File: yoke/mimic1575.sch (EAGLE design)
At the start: 33 parts, among them P1 1K, P2 20, P3 1K, P4 20, U1 CD74HCT75, U10 DG417B, U11 OPA2340N, U12 CD74HCT123, U2 CD74HC573E, U3 CD74HC573E, U4 CD74HC573E, U5 AD7533, U6 AD7533, U7 DG417B, U8 OPA2340N

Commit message: more changes
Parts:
- removed C1, C5: 10pF, keiths:C-0.1
- removed C10, C9: 27pF, keiths:C-0.1
- removed C3, C6: 1000pF, keiths:C-0.1
- removed C7: 3.3uF, keiths:MKS2B043301H00
- removed P1, P3: 1K, keiths:POT-3006P
- removed P2, P4: 20, keiths:POT-3006P
- removed R1, R10: 332, keiths:R-1/4WATT
- removed R16: 1M, keiths:R-1/4WATT
- removed R17, R9: 1.0K, keiths:R-1/4WATT
- removed R4: 2.0K, keiths:R-1/4WATT
- removed U1: CD74HCT75, keiths:CD74HCT75
- removed U10, U7: DG417B, keiths:DG417B
- removed U11, U8: OPA2340N, keiths:OPA2340N
- removed U12: CD74HCT123, keiths:CD74HCT123
- removed U2, U3, U4: CD74HC573E, keiths:CD74HC573E
- removed U5, U6: AD7533, keiths:AD7533
- added C2: 0.022 uF, keiths:ECQ-E2223JF
- added P6: 44PINEDGE, keiths:44PINEDGE
- added Q1, Q14, Q15, Q20, Q6: 2N3904, keiths:2N3904
- added Q10, Q16, Q17, Q18, Q19, Q7: 2N2907, keiths:2N2907
- added Q11, Q13: 2N3906, keiths:2N3906
- added R12: 470, keiths:AXIALRESISTORQUARTER_WATT
- added R13: 560, keiths:AXIALRESISTORQUARTER_WATT
- added R14, R19: 27, keiths:AXIALRESISTORQUARTER_WATT
- added R21: 120, keiths:AXIALRESISTORQUARTER_WATT
- C4: value 3.3uF -> 0.022 uF; device keiths:MKS2B043301H00 -> keiths:ECQ-E2223JF; PN MKS2B043301H00MSSD -> ECQ-E2223JFB
- R11: value 220 -> 1500; device keiths:R-1/4WATT -> keiths:AXIALRESISTORQUARTER_WATT
- R3: value 220 -> 27; device keiths:R-1/4WATT -> keiths:AXIALRESISTORQUARTER_WATT
- R5: value 2.0K -> 27; device keiths:R-1/4WATT -> keiths:AXIALRESISTORQUARTER_WATT
- R8: value 1M -> 120; device keiths:R-1/4WATT -> keiths:AXIALRESISTORQUARTER_WATT
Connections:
- removed net +15V: U10.V+, U11P.V+, U5.VDD, U6.VDD, U7.V+, U8P.V+
- removed net D0: U1.1D1, U1.2D1
- removed net D1: U1.1D0, U1.2D0
- removed net D2: U2.D7, U3.D7, U4.D7
- removed net D3: U2.D6, U3.D6, U4.D6
- removed net D4: U2.D5, U3.D5, U4.D5
- removed net D5: U2.D4, U3.D4, U4.D4
- removed net D6: U2.D3, U3.D3, U4.D3
- removed net D7: U2.D2, U3.D2, U4.D2
- removed net D8: U2.D1, U3.D1, U4.D1
- removed net D9: U2.D0, U3.D0, U4.D0
- removed net LEX: U1.!1LE, U3.LE
- removed net LEX1: U12.1B
- removed net LEY: U1.!2LE, U2.LE
- removed net LEY1: U12.2B
- removed net LE_CTR: U4.LE
- removed net N$1: R9.P$2, U11B.-IN, U11B.OUT
- removed net N$10: U2.Q3, U6.D6
- removed net N$11: U2.Q4, U6.D5
- removed net N$12: U2.Q5, U6.D4
- removed net N$13: U2.Q6, U6.D3
- removed net N$14: U2.Q7, U6.D2
- removed net N$15: U4.Q7
- removed net N$16: U4.Q6
- removed net N$17: U4.Q5
- removed net N$18: U4.Q4
- removed net N$19: U4.Q3
- removed net N$2: C9.2, R4.P$1, U12.1R/C
- removed net N$20: U4.Q2
- removed net N$21: U4.Q1
- removed net N$23: C1.2, R1.P$1, U10.S, U11A.OUT
- removed net N$25: U3.Q0, U5.D9
- removed net N$29: U3.Q4, U5.D5
- removed net N$3: U1.1Q0, U5.D1
- removed net N$4: U1.1Q1, U5.D0
- removed net N$40: C4.1, P2.A, R9.P$1
- removed net N$42: C3.1, R3.P$1, R8.P$1, U11B.+IN
- removed net N$44: C5.2, R10.P$1, U7.S, U8A.OUT
- removed net N$45: C5.1, U6.IO1, U8A.-IN
- removed net N$46: U6.IO2, U8A.+IN
- removed net N$47: R10.P$2, U6.RFB
- removed net N$48: C10.1, U12.2C
- removed net N$49: C6.1, R11.P$1, R16.P$1, U8B.+IN
- removed net N$5: C1.1, U11A.-IN, U5.IO1
- removed net N$50: R17.P$2, U8B.-IN, U8B.OUT
- removed net N$51: R11.P$2, U7.D
- removed net N$53: P3.A, U6.VREF
- removed net N$56: C7.1, P4.A, R17.P$1
- removed net N$6: U11A.+IN, U5.IO2
- removed net N$7: U2.Q0, U6.D9
- removed net N$8: U2.Q1, U6.D8
- removed net N$9: U2.Q2, U6.D7
- removed net VREF: P1.E, P1.S, P3.E, P3.S
- removed net XOUT: C4.2, P2.E, P2.S
- removed net X_GATE: U10.IN, U12.1Q
- removed net YOUT: C7.2, P4.E, P4.S
- removed net Y_GATE: U12.2Q, U7.IN
- new net +10V: P6.A, R12.P$2, R19.P$2, R5.P$2, R8.P$2
- new net +50V: P6.E
- new net GATE: Q20.B
- new net INPUT: Q7.B
- new net W_IN: P6.W
- new net Z_IN: P6.Z
- net +5V: now also P6.F; no longer R4.P$2, R5.P$2, U1.+5V, U10.VL, U12.!1CLR, U12.!2CLR, U12.+5V, U2.+5V, U3.+5V, U4.+5V, U7.VL
- net -15V: now also C2.1, C4.1, P6.C, R13.P$1, R14.P$1, R21.P$1, R3.P$1; no longer U10.V-, U11P.V-, U7.V-, U8P.V-
- net GND: now also P6.D; no longer C3.2, C6.2, R16.P$2, R8.P$2, U1.GND, U10.GND, U12.!1A, U12.!2A, U12.GND, U2.!OE, U2.GND, U3.!OE, U3.GND, U4.!OE, U4.GND, U5.GND, U6.GND, U7.GND
- net N$22: now also Q14.B, Q6.B; no longer U4.Q0
- net N$24: now also Q17.E, R5.P$1; no longer P1.A, U5.VREF
- net N$26: now also Q18.E, R8.P$1; no longer U3.Q1, U5.D8
- net N$27: now also Q14.E, R3.P$2; no longer U3.Q2, U5.D7
- net N$28: now also Q6.E, R14.P$2; no longer U3.Q3, U5.D6
- net N$30: now also Q18.C, Q19.B, Q7.E; no longer U3.Q5, U5.D4
- net N$31: now also C2.2, Q7.C, R13.P$2; no longer U3.Q6, U5.D3
- net N$32: now also Q10.B, Q14.C, Q17.B, Q17.C, Q18.B; no longer U3.Q7, U5.D2
- net N$33: now also Q10.E, R19.P$1; no longer C9.1, U12.1C
- net N$34: now also Q6.C, R11.P$1; no longer R3.P$2, U10.D
- net N$35: now also Q10.C, Q19.E; no longer U1.2Q0, U6.D1
- net N$36: now also C4.2, Q19.C, R21.P$2; no longer U1.2Q1, U6.D0
- net N$37: now also Q20.E, R11.P$2; no longer C10.2, R5.P$1, U12.2R/C
- net N$38: now also Q20.C, R12.P$1; no longer R1.P$2, U5.RFB
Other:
- note added: "Follow and Hold"

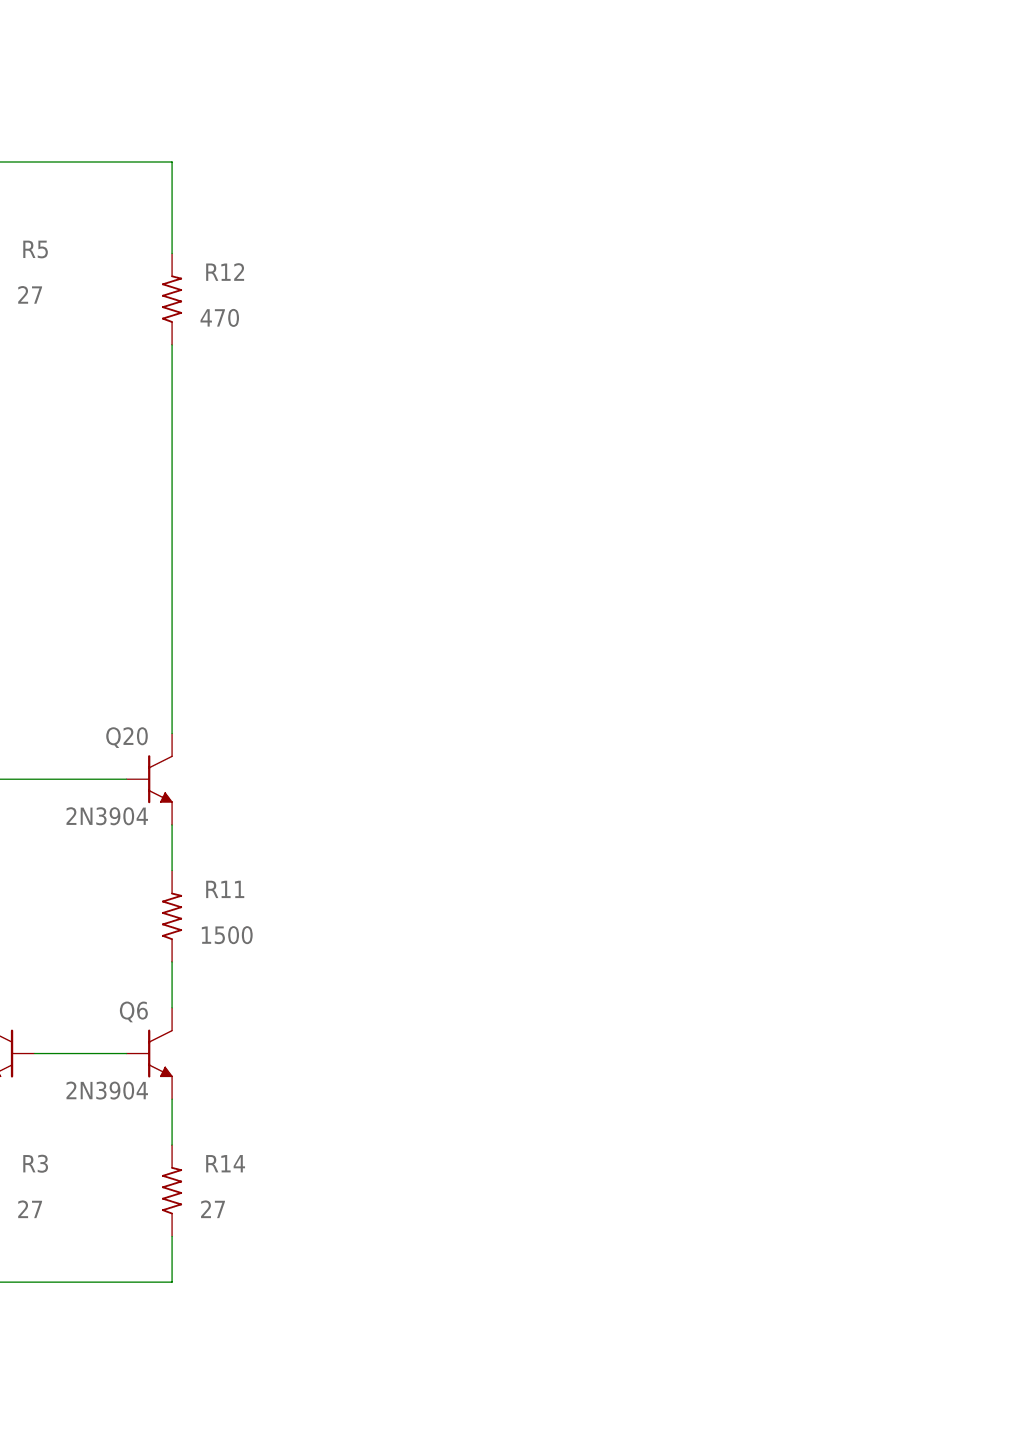
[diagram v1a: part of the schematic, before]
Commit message: LTspice files added
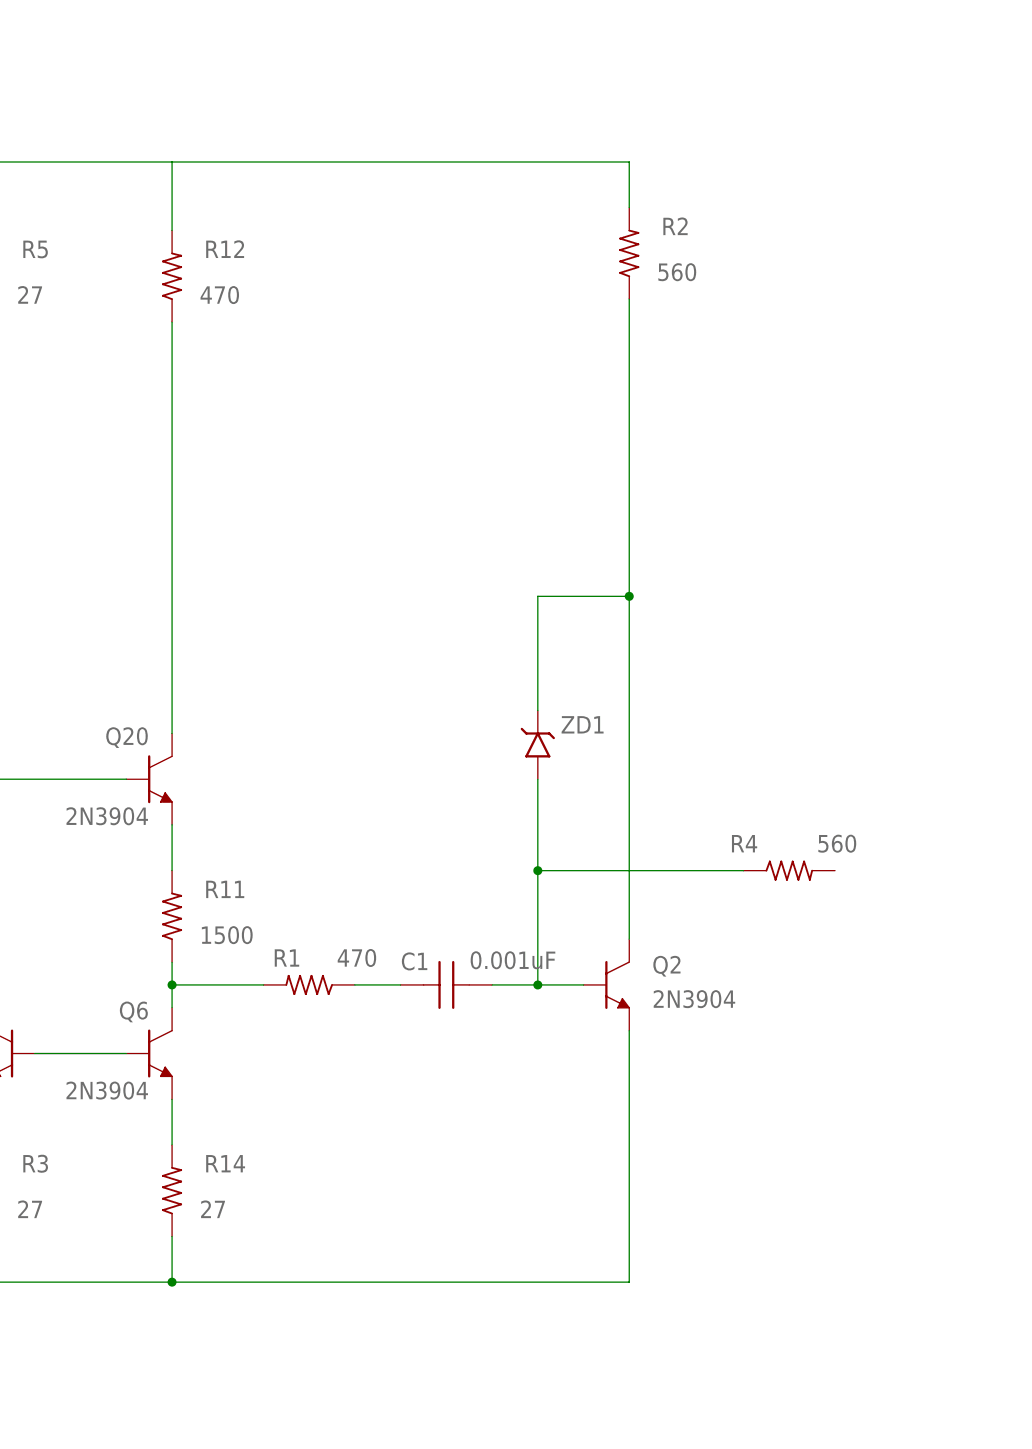
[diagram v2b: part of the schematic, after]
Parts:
- added C1: 0.001uF, keiths:CAP0.1UF100V
- added Q2: 2N3904, keiths:2N3904
- added R1: 470, keiths:AXIALRESISTORQUARTER_WATT
- added R2, R4: 560, keiths:AXIALRESISTORQUARTER_WATT
- added ZD1: (no value), keiths:1N754A
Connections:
- new net N$1: C1.1, R1.P$1
- new net N$2: Q2.C, R2.P$1, ZD1.C
- new net N$3: C1.2, Q2.B, R4.P$1, ZD1.A
- net +10V: now also R2.P$2
- net -15V: now also Q2.E
- net N$34: now also R1.P$2
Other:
- moved on the sheet: R12
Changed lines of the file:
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@@
 <attribute name="PN" value="2N3904"/>
 </part>
+<part name="C1" library="keiths" deviceset="CAP0.1UF100V" device="" value="0.001uF"/>
+<part name="R1" library="keiths" deviceset="AXIALRESISTOR" device="QUARTER_WATT" value="470"/>
+<part name="Q2" library="keiths" deviceset="2N3904" device="">
+<attribute name="PN" value="2N3904"/>
+</part>
+<part name="R2" library="keiths" deviceset="AXIALRESISTOR" device="QUARTER_WATT" value="560"/>
+<part name="ZD1" library="keiths" deviceset="1N754A" device=""/>
+<part name="R4" library="keiths" deviceset="AXIALRESISTOR" device="QUARTER_WATT" value="560"/>
 </parts>
 <sheets>
@@
 <attribute name="VALUE" x="229.108" y="182.372" size="1.9304" layer="96" font="vector" ratio="10"/>
 </instance>
-<instance part="R12" gate="G$1" x="226.06" y="254" smashed="yes" rot="R180">
-<attribute name="NAME" x="229.616" y="256.032" size="1.9304" layer="95" font="vector" ratio="10"/>
-<attribute name="VALUE" x="229.108" y="250.952" size="1.9304" layer="96" font="vector" ratio="10"/>
+<instance part="R12" gate="G$1" x="226.06" y="256.54" smashed="yes" rot="R180">
+<attribute name="NAME" x="229.616" y="258.572" size="1.9304" layer="95" font="vector" ratio="10"/>
+<attribute name="VALUE" x="229.108" y="253.492" size="1.9304" layer="96" font="vector" ratio="10"/>
 </instance>
 <instance part="R14" gate="G$1" x="226.06" y="154.94" smashed="yes" rot="R180">
@@
 <attribute name="VALUE" x="162.56" y="289.56" size="1.9304" layer="96" font="vector" ratio="10"/>
 <attribute name="PN" x="154.94" y="294.64" size="1.778" layer="96" display="off"/>
+</instance>
+<instance part="C1" gate="G$1" x="256.54" y="177.8" smashed="yes" rot="R90">
+<attribute name="NAME" x="251.46" y="179.451" size="1.9304" layer="95" font="vector" ratio="10"/>
+<attribute name="VALUE" x="259.08" y="179.578" size="1.9304" layer="96" font="vector" ratio="10"/>
+</instance>
+<instance part="R1" gate="G$1" x="241.3" y="177.8" smashed="yes" rot="R270">
+<attribute name="NAME" x="237.236" y="179.832" size="1.9304" layer="95" font="vector" ratio="10"/>
+<attribute name="VALUE" x="244.348" y="179.832" size="1.9304" layer="96" font="vector" ratio="10"/>
+</instance>
+<instance part="Q2" gate="G1" x="274.32" y="177.8" smashed="yes">
+<attribute name="NAME" x="279.4" y="179.07" size="1.9304" layer="95" font="vector" ratio="10"/>
+<attribute name="VALUE" x="279.4" y="175.26" size="1.9304" layer="96" font="vector" ratio="10"/>
+<attribute name="PN" x="274.32" y="177.8" size="1.778" layer="96" display="off"/>
+</instance>
+<instance part="R2" gate="G$1" x="276.86" y="259.08" smashed="yes" rot="R180">
+<attribute name="NAME" x="280.416" y="261.112" size="1.9304" layer="95" font="vector" ratio="10"/>
+<attribute name="VALUE" x="279.908" y="256.032" size="1.9304" layer="96" font="vector" ratio="10"/>
+</instance>
+<instance part="ZD1" gate="G$1" x="266.7" y="203.2"/>
+<instance part="R4" gate="G$1" x="294.64" y="190.5" smashed="yes" rot="R90">
+<attribute name="NAME" x="288.036" y="192.532" size="1.9304" layer="95" font="vector" ratio="10"/>
+<attribute name="VALUE" x="297.688" y="192.532" size="1.9304" layer="96" font="vector" ratio="10"/>
 </instance>
 </instances>
@@
 <wire x1="205.74" y1="149.86" x2="205.74" y2="144.78" width="0.1524" layer="91"/>
 <junction x="205.74" y="144.78"/>
+<pinref part="Q2" gate="G1" pin="E"/>
+<wire x1="226.06" y1="144.78" x2="276.86" y2="144.78" width="0.1524" layer="91"/>
+<wire x1="276.86" y1="144.78" x2="276.86" y2="172.72" width="0.1524" layer="91"/>
+<junction x="226.06" y="144.78"/>
 </segment>
 </net>
@@
 <wire x1="170.18" y1="269.24" x2="205.74" y2="269.24" width="0.1524" layer="91"/>
 <wire x1="205.74" y1="269.24" x2="226.06" y2="269.24" width="0.1524" layer="91"/>
-<wire x1="226.06" y1="269.24" x2="226.06" y2="259.08" width="0.1524" layer="91"/>
 <junction x="170.18" y="269.24"/>
 <pinref part="R5" gate="G$1" pin="P$2"/>
+<wire x1="226.06" y1="269.24" x2="226.06" y2="261.62" width="0.1524" layer="91"/>
 <wire x1="205.74" y1="261.62" x2="205.74" y2="269.24" width="0.1524" layer="91"/>
 <junction x="205.74" y="269.24"/>
+<pinref part="R2" gate="G$1" pin="P$2"/>
+<wire x1="276.86" y1="264.16" x2="276.86" y2="269.24" width="0.1524" layer="91"/>
+<wire x1="276.86" y1="269.24" x2="226.06" y2="269.24" width="0.1524" layer="91"/>
 </segment>
 </net>
@@
 <pinref part="Q6" gate="G1" pin="C"/>
 <pinref part="R11" gate="G$1" pin="P$1"/>
-<wire x1="226.06" y1="175.26" x2="226.06" y2="180.34" width="0.1524" layer="91"/>
+<wire x1="226.06" y1="175.26" x2="226.06" y2="177.8" width="0.1524" layer="91"/>
+<pinref part="R1" gate="G$1" pin="P$2"/>
+<wire x1="226.06" y1="177.8" x2="226.06" y2="180.34" width="0.1524" layer="91"/>
+<wire x1="236.22" y1="177.8" x2="226.06" y2="177.8" width="0.1524" layer="91"/>
+<junction x="226.06" y="177.8"/>
 </segment>
 </net>
@@
 <pinref part="Q20" gate="G1" pin="C"/>
 <pinref part="R12" gate="G$1" pin="P$1"/>
-<wire x1="226.06" y1="248.92" x2="226.06" y2="205.74" width="0.1524" layer="91"/>
+<wire x1="226.06" y1="251.46" x2="226.06" y2="205.74" width="0.1524" layer="91"/>
 </segment>
 </net>
@@
 </segment>
 </net>
+<net name="N$1" class="0">
+<segment>
+<pinref part="C1" gate="G$1" pin="1"/>
+<pinref part="R1" gate="G$1" pin="P$1"/>
+<wire x1="246.38" y1="177.8" x2="251.46" y2="177.8" width="0.1524" layer="91"/>
+</segment>
+</net>
+<net name="N$3" class="0">
+<segment>
+<pinref part="C1" gate="G$1" pin="2"/>
+<pinref part="Q2" gate="G1" pin="B"/>
+<wire x1="271.78" y1="177.8" x2="266.7" y2="177.8" width="0.1524" layer="91"/>
+<wire x1="266.7" y1="177.8" x2="261.62" y2="177.8" width="0.1524" layer="91"/>
+<wire x1="266.7" y1="177.8" x2="266.7" y2="190.5" width="0.1524" layer="91"/>
+<junction x="266.7" y="177.8"/>
+<pinref part="ZD1" gate="G$1" pin="A"/>
+<wire x1="266.7" y1="190.5" x2="266.7" y2="200.66" width="0.1524" layer="91"/>
+<wire x1="266.7" y1="190.5" x2="289.56" y2="190.5" width="0.1524" layer="91"/>
+<junction x="266.7" y="190.5"/>
+<pinref part="R4" gate="G$1" pin="P$1"/>
+</segment>
+</net>
+<net name="N$2" class="0">
+<segment>
+<pinref part="ZD1" gate="G$1" pin="C"/>
+<wire x1="266.7" y1="208.28" x2="266.7" y2="220.98" width="0.1524" layer="91"/>
+<pinref part="Q2" gate="G1" pin="C"/>
+<pinref part="R2" gate="G$1" pin="P$1"/>
+<wire x1="276.86" y1="182.88" x2="276.86" y2="220.98" width="0.1524" layer="91"/>
+<wire x1="276.86" y1="220.98" x2="276.86" y2="254" width="0.1524" layer="91"/>
+<wire x1="266.7" y1="220.98" x2="276.86" y2="220.98" width="0.1524" layer="91"/>
+<junction x="276.86" y="220.98"/>
+</segment>
+</net>

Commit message: update netlist
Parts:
- removed Q17, Q18: 2N2907, keiths:2N2907
- added C10: 0.1uF, keiths:CAP0.1UF100V
- added C11: 3.3 UF, keiths:ECW-FD2W335K
- added C3: 56 pF, keiths:CAP0.1UF100V
- added C5: 680pF, keiths:CAP0.1UF100V
- added C6: 330pF, keiths:CAP0.1UF100V
- added C7: 120pF, keiths:CAP0.1UF100V
- added C8, C9: 0.022 uF, keiths:ECQ-E2223JF
- added D1, D2: 1N4148, keiths:1N4148
- added P1: 20, keiths:POT-3006P
- added Q12, Q3, Q4, Q8: 2N3904, keiths:2N3904
- added Q21, Q22, Q9: 2N3906, keiths:2N3906
- added Q5: 2N2222A, keiths:2N2222A
- added R10, R27, R30, R6: 1 K, keiths:AXIALRESISTORQUARTER_WATT
- added R15, R26, R31: 120, keiths:AXIALRESISTORQUARTER_WATT
- added R16, R17, R7, R9: 560, keiths:AXIALRESISTORQUARTER_WATT
- added R18, R20, R25, R28: 27, keiths:AXIALRESISTORQUARTER_WATT
- added R22: 1.5 K, keiths:AXIALRESISTORQUARTER_WATT
- added R23: 10 K, keiths:AXIALRESISTORQUARTER_WATT
- added R24: 680, keiths:AXIALRESISTORQUARTER_WATT
- added R29: 330, keiths:AXIALRESISTORQUARTER_WATT
- added ZD2: BAT43, keiths:1N754A
- added ZD3: (no value), keiths:1N754A
- C1: MPN (none) -> 1000 pf
- Q10, Q7: value 2N2907 -> 2N3906; device keiths:2N2907 -> keiths:2N3906; PN 2N2907A -> (none)
- Q11, Q13: value 2N3906 -> 2N3904; device keiths:2N3906 -> keiths:2N3904; PN 2N3906 -> 2N3904
- Q14: value 2N3904 -> 2N3906; device keiths:2N3904 -> keiths:2N3906; PN 2N3904 -> (none)
- Q16: value 2N2907 -> 2N2222A; device keiths:2N2907 -> keiths:2N2222A; PN 2N2907A -> (none)
- R1: value 470 -> 220
- R3: value 27 -> 680
- R4: value 560 -> 120
- ZD1: value (none) -> BAT43; PN (none) -> BAT43
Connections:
- removed net +50V: P6.E
- removed net +5V: P6.F
- removed net GATE: Q20.B
- removed net INPUT: Q7.B
- removed net N$32: Q10.B, Q14.C, Q17.B, Q17.C, Q18.B
- removed net N$35: Q10.C, Q19.E
- removed net W_IN: P6.W
- removed net Z_IN: P6.Z
- new net +10V1: Q5.C, R10.P$2, R12.P$2, R16.P$2, R19.P$2, R2.P$2, R20.P$2, R25.P$2, R5.P$2, R8.P$2, R9.P$2
- new net E_IN: P6.E, R31.P$2
- new net H_IN: C10.1, C11.1, P1.1, P6.H, R30.P$1
- new net K_IN: P6.K, Q20.B
- new net N$10: Q9.E, R20.P$1
- new net N$11: Q4.C, Q5.B, R16.P$1, R23.P$2, ZD3.C
- new net N$12: Q4.B, R15.P$2, ZD3.A
- new net N$14: Q11.B, Q15.B, Q21.C, Q6.B, Q8.B, Q8.C
- new net N$15: Q1.C, Q10.C, Q12.E, Q19.E
- new net N$16: Q22.E, R25.P$1
- new net N$17: Q12.B, R3.P$1
- new net N$18: Q11.E, R26.P$2
- new net N$19: Q1.B, R24.P$1
- new net N$20: C7.1, Q1.E, Q12.C, Q13.B
- new net N$21: Q10.B, Q14.B, Q21.B, Q22.B, Q9.B, Q9.C, R27.P$2
- new net N$23: D2.A, Q22.C, R24.P$2, R3.P$2
- new net N$25: Q7.B, R31.P$1
- new net N$36: Q15.E, R28.P$2
- new net N$39: Q15.C, Q16.E, R30.P$2
- new net N$4: C3.1, R15.P$1, R4.P$2, R6.P$2
- new net N$40: C9.2, Q16.C, R29.P$1
- new net N$5: C3.2, Q3.C, R10.P$1, R6.P$1, ZD2.C
- new net N$6: D2.C, Q5.E, R17.P$2
- new net N$7: Q8.E, R18.P$2
- new net N$8: D1.C, Q3.B, ZD2.A
- new net N$9: C5.2, C6.2, D1.A, R7.P$2, R9.P$1
- new net Z_OUT: C10.2, C11.2, P1.2, P1.3, P6.Z
- net +10V: now also R22.P$2, R29.P$2; no longer R12.P$2, R19.P$2, R2.P$2, R5.P$2, R8.P$2
- net -15V: now also Q3.E, Q4.E, R17.P$1, R18.P$1, R23.P$1, R26.P$1, R28.P$1, R7.P$1; no longer C2.1, C4.1, R3.P$1
- net GND: now also C2.1, C4.1, C7.2, C8.1, C9.1, R27.P$1
- net N$2: now also C5.1, C6.1
- net N$22: now also Q11.C, Q13.E, Q16.B; no longer Q14.B, Q6.B
- net N$24: now also Q21.E; no longer Q17.E
- net N$26: now also Q14.E; no longer Q18.E
- net N$27: now also C8.2, Q13.C, R22.P$1; no longer Q14.E, R3.P$2
- net N$30: now also Q14.C; no longer Q18.C
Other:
- note added: "Closed Loop Input"
- note added: "Compensation network, 20 ohms in parallel with 3.4 u Farads."
- note added: "Follow Hold and Compensation"
- note added: "Gate Input"
- note added: "Open Loop Input"
- note added: "Output to Current Amplifier"
- note removed: "Follow and Hold"
- moved on the sheet: C1, C2, C4, P6, Q1, Q10, Q15, Q19, Q2, Q20, Q6, Q7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
